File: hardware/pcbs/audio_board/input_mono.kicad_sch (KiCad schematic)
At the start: 3 parts, among them J7 Stereo Line-in

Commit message: fix libraries
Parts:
- renumbered J7 to J10, R6 to R53, R28 to R54
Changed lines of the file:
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@@
 		(dnp no)
 		(fields_autoplaced yes)
-		(property "Reference" "#PWR023"
+		(property "Reference" "#PWR0114"
 			(at 93.98 106.68 0)
 			(effects
@@
 			(project "audio_board"
 				(path "/54443f96-c7c5-4432-b890-45b14a1547a1/c7838b89-33be-4400-baf7-0a033ee6e87f"
-					(reference "#PWR023")
+					(reference "#PWR0114")
 					(unit 1)
 				)
@@
 		(dnp no)
 		(fields_autoplaced yes)
-		(property "Reference" "R6"
+		(property "Reference" "R53"
 			(at 105.41 89.9541 90)
 			(effects
@@
 			(project "audio_board"
 				(path "/54443f96-c7c5-4432-b890-45b14a1547a1/c7838b89-33be-4400-baf7-0a033ee6e87f"
-					(reference "R6")
+					(reference "R53")
 					(unit 1)
 				)
@@
 		(on_board yes)
 		(dnp no)
-		(property "Reference" "J7"
+		(property "Reference" "J10"
 			(at 80.645 103.3399 0)
 			(effects
@@
 			(project "audio_board"
 				(path "/54443f96-c7c5-4432-b890-45b14a1547a1/c7838b89-33be-4400-baf7-0a033ee6e87f"
-					(reference "J7")
+					(reference "J10")
 					(unit 1)
 				)
@@
 		(on_board yes)
 		(dnp no)
-		(property "Reference" "R28"
+		(property "Reference" "R54"
 			(at 105.41 100.5459 90)
 			(effects
@@
 			(project "audio_board"
 				(path "/54443f96-c7c5-4432-b890-45b14a1547a1/c7838b89-33be-4400-baf7-0a033ee6e87f"
-					(reference "R28")
+					(reference "R54")
 					(unit 1)
 				)

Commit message: some more routing
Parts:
- renumbered R53 to R54, R54 to R55
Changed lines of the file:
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@@
 		(dnp no)
 		(fields_autoplaced yes)
-		(property "Reference" "#PWR0114"
+		(property "Reference" "#PWR0115"
 			(at 93.98 106.68 0)
 			(effects
@@
 			(project "audio_board"
 				(path "/54443f96-c7c5-4432-b890-45b14a1547a1/c7838b89-33be-4400-baf7-0a033ee6e87f"
-					(reference "#PWR0114")
+					(reference "#PWR0115")
 					(unit 1)
 				)
@@
 		(dnp no)
 		(fields_autoplaced yes)
-		(property "Reference" "R53"
+		(property "Reference" "R54"
 			(at 105.41 89.9541 90)
 			(effects
@@
 			(project "audio_board"
 				(path "/54443f96-c7c5-4432-b890-45b14a1547a1/c7838b89-33be-4400-baf7-0a033ee6e87f"
-					(reference "R53")
+					(reference "R54")
 					(unit 1)
 				)
@@
 		(on_board yes)
 		(dnp no)
-		(property "Reference" "R54"
+		(property "Reference" "R55"
 			(at 105.41 100.5459 90)
 			(effects
@@
 			(project "audio_board"
 				(path "/54443f96-c7c5-4432-b890-45b14a1547a1/c7838b89-33be-4400-baf7-0a033ee6e87f"
-					(reference "R54")
+					(reference "R55")
 					(unit 1)
 				)

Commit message: route some more
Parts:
- added R54: 510, Resistor_SMD:R_0805_2012Metric, symbol Device:R
- renumbered R54 to R55, R55 to R56
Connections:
- net GND: now also R54.1; no longer J10.S
- net OUTPUT renamed OUT+
- new net OUT-: J10.S, R54.2
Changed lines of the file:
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@@
 		(color 0 0 0 0)
 	)
+	(junction
+		(at 99.06 104.14)
+		(diameter 0)
+		(color 0 0 0 0)
+	)
+	(wire
+		(pts
+			(xy 99.06 104.14) (xy 121.92 104.14)
+		)
+		(stroke
+			(width 0)
+			(type default)
+		)
+	)
+	(wire
+		(pts
+			(xy 99.06 99.06) (xy 99.06 104.14)
+		)
+		(stroke
+			(width 0)
+			(type default)
+		)
+	)
 	(wire
 		(pts
@@
 	(wire
 		(pts
-			(xy 87.63 99.06) (xy 93.98 99.06)
+			(xy 87.63 99.06) (xy 99.06 99.06)
 		)
 		(stroke
@@
 	(wire
 		(pts
+			(xy 99.06 104.14) (xy 99.06 106.68)
+		)
+		(stroke
+			(width 0)
+			(type default)
+		)
+	)
+	(wire
+		(pts
+			(xy 99.06 114.3) (xy 99.06 115.57)
+		)
+		(stroke
+			(width 0)
+			(type default)
+		)
+	)
+	(wire
+		(pts
 			(xy 114.3 96.52) (xy 114.3 95.25)
 		)
@@
 	(wire
 		(pts
-			(xy 93.98 99.06) (xy 93.98 100.33)
-		)
-		(stroke
-			(width 0)
-			(type default)
-		)
-	)
-	(wire
-		(pts
 			(xy 87.63 93.98) (xy 101.6 93.98)
 		)
@@
 		)
 	)
-	(hierarchical_label "OUTPUT"
+	(hierarchical_label "OUT+"
 		(shape output)
 		(at 121.92 95.25 0)
@@
 		)
 	)
+	(hierarchical_label "OUT-"
+		(shape output)
+		(at 121.92 104.14 0)
+		(effects
+			(font
+				(size 1.27 1.27)
+			)
+			(justify left)
+		)
+	)
 	(symbol
 		(lib_id "power:GND")
-		(at 93.98 100.33 0)
+		(at 99.06 115.57 0)
 		(unit 1)
 		(exclude_from_sim no)
@@
 		(fields_autoplaced yes)
 		(property "Reference" "#PWR0115"
-			(at 93.98 106.68 0)
+			(at 99.06 121.92 0)
 			(effects
 				(font
@@
 		)
 		(property "Value" "GND"
-			(at 93.98 104.4655 0)
-			(effects
-				(font
-					(size 1.27 1.27)
-				)
+			(at 99.06 119.7055 0)
+			(effects
+				(font
+					(size 1.27 1.27)
+				)
+				(hide yes)
 			)
 		)
 		(property "Footprint" ""
-			(at 93.98 100.33 0)
+			(at 99.06 115.57 0)
 			(effects
 				(font
@@
 		)
 		(property "Datasheet" ""
-			(at 93.98 100.33 0)
+			(at 99.06 115.57 0)
 			(effects
 				(font
@@
 		)
 		(property "Description" ""
-			(at 93.98 100.33 0)
+			(at 99.06 115.57 0)
 			(effects
 				(font
@@
 		(dnp no)
 		(fields_autoplaced yes)
-		(property "Reference" "R54"
+		(property "Reference" "R55"
 			(at 105.41 89.9541 90)
 			(effects
@@
 			(project "audio_board"
 				(path "/54443f96-c7c5-4432-b890-45b14a1547a1/c7838b89-33be-4400-baf7-0a033ee6e87f"
-					(reference "R54")
+					(reference "R55")
 					(unit 1)
 				)
@@
 		(on_board yes)
 		(dnp no)
-		(property "Reference" "R55"
+		(property "Reference" "R56"
 			(at 105.41 100.5459 90)
 			(effects
@@
 			(project "audio_board"
 				(path "/54443f96-c7c5-4432-b890-45b14a1547a1/c7838b89-33be-4400-baf7-0a033ee6e87f"
-					(reference "R55")
+					(reference "R56")
 					(unit 1)
 				)
+			)
+		)
+	)
+	(symbol
+		(lib_id "Device:R")
+		(at 99.06 110.49 0)
+		(mirror x)
+		(unit 1)
+		(exclude_from_sim no)
+		(in_bom yes)
+		(on_board yes)
+		(dnp no)
+		(property "Reference" "R54"
+			(at 103.0859 110.49 90)
+			(effects
+				(font
+					(size 1.27 1.27)
+				)
+			)
+		)
+		(property "Value" "510"
+			(at 101.1649 110.49 90)
+			(effects
+				(font
+					(size 1.27 1.27)
+				)
+			)
+		)
+		(property "Footprint" "Resistor_SMD:R_0805_2012Metric"
+			(at 97.282 110.49 90)
+			(effects
+				(font
+					(size 1.27 1.27)
+				)
+				(hide yes)
+			)
+		)
+		(property "Datasheet" "~"
+			(at 99.06 110.49 0)
+			(effects
+				(font
+					(size 1.27 1.27)
+				)
+				(hide yes)
+			)
+		)
+		(property "Description" ""
+			(at 99.06 110.49 0)
+			(effects
+				(font
+					(size 1.27 1.27)
+				)
+				(hide yes)
+			)
+		)
+		(property "LCSC" "C25804"
+			(at 99.06 110.49 0)
+			(effects
+				(font
+					(size 1.27 1.27)
+				)
+				(hide yes)
+			)
+		)
+		(property "Part" "R 10kΩ 125mW 1% 0603"
+			(at 99.06 110.49 0)
+			(effects
+				(font
+					(size 1.27 1.27)
+				)
+				(hide yes)
+			)
+		)
+		(property "MPN" "560112116023 "
+			(at 99.06 110.49 0)
+			(effects
+				(font
+					(size 1.27 1.27)
+				)
+				(hide yes)
+			)
+		)
+		(property "Shop" "https://store.comet.bg/Catalogue/Product/4415/"
+			(at 99.06 110.49 0)
+			(effects
+				(font
+					(size 1.27 1.27)
+				)
+				(hide yes)
+			)
+		)
+		(pin "1"
+		)
+		(pin "2"
+		)
+		(instances
+			(project "audio_board"
+				(path "/54443f96-c7c5-4432-b890-45b14a1547a1/c7838b89-33be-4400-baf7-0a033ee6e87f"
+					(reference "R54")
+					(unit 1)
+				)

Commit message: finish routing
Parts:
- renumbered R54 to R53, R55 to R54, R56 to R55
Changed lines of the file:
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@@
 		(dnp no)
 		(fields_autoplaced yes)
-		(property "Reference" "R55"
+		(property "Reference" "R54"
 			(at 105.41 89.9541 90)
 			(effects
@@
 			(project "audio_board"
 				(path "/54443f96-c7c5-4432-b890-45b14a1547a1/c7838b89-33be-4400-baf7-0a033ee6e87f"
-					(reference "R55")
+					(reference "R54")
 					(unit 1)
 				)
@@
 		(on_board yes)
 		(dnp no)
-		(property "Reference" "R56"
+		(property "Reference" "R55"
 			(at 105.41 100.5459 90)
 			(effects
@@
 			(project "audio_board"
 				(path "/54443f96-c7c5-4432-b890-45b14a1547a1/c7838b89-33be-4400-baf7-0a033ee6e87f"
-					(reference "R56")
+					(reference "R55")
 					(unit 1)
 				)
@@
 		(on_board yes)
 		(dnp no)
-		(property "Reference" "R54"
+		(property "Reference" "R53"
 			(at 103.0859 110.49 90)
 			(effects
@@
 			(project "audio_board"
 				(path "/54443f96-c7c5-4432-b890-45b14a1547a1/c7838b89-33be-4400-baf7-0a033ee6e87f"
-					(reference "R54")
+					(reference "R53")
 					(unit 1)
 				)

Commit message: component values
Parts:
- J10: Part SJ1-3533NG -> (none); Shop https://eu.mouser.com/ProductDetail/490-SJ1-3533NG -> (none)
- R53, R54, R55: LCSC C25804 -> (none); MPN 560112116023 -> (none); Part R 10kΩ 125mW 1% 0603 -> (none); Shop https://store.comet.bg/Catalogue/Product/4415/ -> (none)
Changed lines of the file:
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@@
 			)
 		)
-		(property "LCSC" "C25804"
-			(at 105.41 93.98 0)
-			(effects
-				(font
-					(size 1.27 1.27)
-				)
-				(hide yes)
-			)
-		)
-		(property "Part" "R 10kΩ 125mW 1% 0603"
-			(at 105.41 93.98 0)
-			(effects
-				(font
-					(size 1.27 1.27)
-				)
-				(hide yes)
-			)
-		)
-		(property "MPN" "560112116023 "
-			(at 105.41 93.98 0)
-			(effects
-				(font
-					(size 1.27 1.27)
-				)
-				(hide yes)
-			)
-		)
-		(property "Shop" "https://store.comet.bg/Catalogue/Product/4415/"
+		(property "MPN" ""
 			(at 105.41 93.98 0)
 			(effects
@@
 			)
 		)
-		(property "Part" " SJ1-3533NG "
-			(at 82.55 96.52 0)
-			(effects
-				(font
-					(size 1.27 1.27)
-				)
-				(hide yes)
-			)
-		)
-		(property "Shop" "https://eu.mouser.com/ProductDetail/490-SJ1-3533NG"
-			(at 82.55 96.52 0)
-			(effects
-				(font
-					(size 1.27 1.27)
-				)
-				(hide yes)
-			)
-		)
 		(pin "R"
 		)
@@
 			)
 		)
-		(property "LCSC" "C25804"
-			(at 105.41 96.52 0)
-			(effects
-				(font
-					(size 1.27 1.27)
-				)
-				(hide yes)
-			)
-		)
-		(property "Part" "R 10kΩ 125mW 1% 0603"
-			(at 105.41 96.52 0)
-			(effects
-				(font
-					(size 1.27 1.27)
-				)
-				(hide yes)
-			)
-		)
-		(property "MPN" "560112116023 "
-			(at 105.41 96.52 0)
-			(effects
-				(font
-					(size 1.27 1.27)
-				)
-				(hide yes)
-			)
-		)
-		(property "Shop" "https://store.comet.bg/Catalogue/Product/4415/"
+		(property "MPN" ""
 			(at 105.41 96.52 0)
 			(effects
@@
 			)
 		)
-		(property "LCSC" "C25804"
+		(property "MPN" ""
 			(at 99.06 110.49 0)
 			(effects
-				(font
-					(size 1.27 1.27)
-				)
-				(hide yes)
-			)
-		)
-		(property "Part" "R 10kΩ 125mW 1% 0603"
-			(at 99.06 110.49 0)
-			(effects
-				(font
-					(size 1.27 1.27)
-				)
-				(hide yes)
-			)
-		)
-		(property "MPN" "560112116023 "
-			(at 99.06 110.49 0)
-			(effects
-				(font
-					(size 1.27 1.27)
-				)
-				(hide yes)
-			)
-		)
-		(property "Shop" "https://store.comet.bg/Catalogue/Product/4415/"
-			(at 99.06 110.49 0)
-			(effects

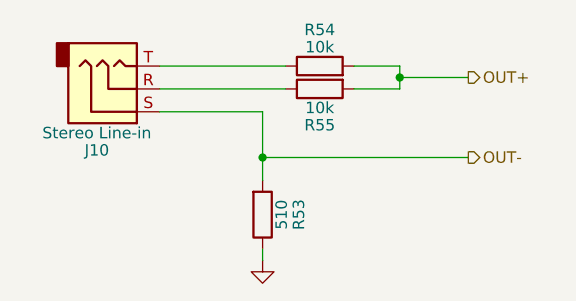
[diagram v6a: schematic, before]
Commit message: revise BOM
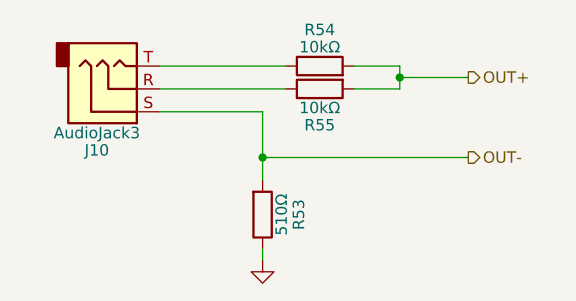
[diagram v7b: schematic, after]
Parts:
- J10: value Stereo Line-in -> AudioJack3; Purpose (none) -> Stereo Line-in
- R53: value 510 -> 510Ω; MPN (none) -> R 510Ω 125mW 1% 0805
- R54, R55: value 10k -> 10kΩ; MPN (none) -> R 10kΩ 125mW 1% 0805
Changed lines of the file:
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@@
 			)
 		)
-		(property "Value" "10k"
+		(property "Value" "10kΩ"
 			(at 105.41 91.8751 90)
 			(effects
@@
 			)
 		)
-		(property "MPN" ""
+		(property "MPN" "R 10kΩ 125mW 1% 0805"
 			(at 105.41 93.98 0)
 			(effects
@@
 			)
 		)
-		(property "Value" "Stereo Line-in"
+		(property "Value" "AudioJack3"
 			(at 80.645 101.4189 0)
 			(effects
@@
 		)
 		(property "MPN" "490-SJ1-3533NG"
+			(at 82.55 96.52 0)
+			(effects
+				(font
+					(size 1.27 1.27)
+				)
+				(hide yes)
+			)
+		)
+		(property "Purpose" "Stereo Line-in"
 			(at 82.55 96.52 0)
 			(effects
@@
 			)
 		)
-		(property "Value" "10k"
+		(property "Value" "10kΩ"
 			(at 105.41 98.6249 90)
 			(effects
@@
 			)
 		)
-		(property "MPN" ""
+		(property "MPN" "R 10kΩ 125mW 1% 0805"
 			(at 105.41 96.52 0)
 			(effects
@@
 			)
 		)
-		(property "Value" "510"
+		(property "Value" "510Ω"
 			(at 101.1649 110.49 90)
 			(effects
@@
 			)
 		)
-		(property "MPN" ""
+		(property "MPN" "R 510Ω 125mW 1% 0805"
 			(at 99.06 110.49 0)
 			(effects

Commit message: fix all silkscreens
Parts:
- J10: footprint Connector_Audio:Jack_3.5mm_CUI_SJ1-3533NG_Horizontal_CircularHoles -> conn:Jack_3.5mm_CUI_SJ1-3533NG_Horizontal_CircularHoles
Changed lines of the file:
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@@
 			)
 		)
-		(property "Footprint" "Connector_Audio:Jack_3.5mm_CUI_SJ1-3533NG_Horizontal_CircularHoles"
+		(property "Footprint" "conn:Jack_3.5mm_CUI_SJ1-3533NG_Horizontal_CircularHoles"
 			(at 82.55 96.52 0)
 			(effects
